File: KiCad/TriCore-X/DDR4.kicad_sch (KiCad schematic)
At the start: 2 parts, among them U1 RK3568B2, U8 IS43LQ32256AL-062BLI

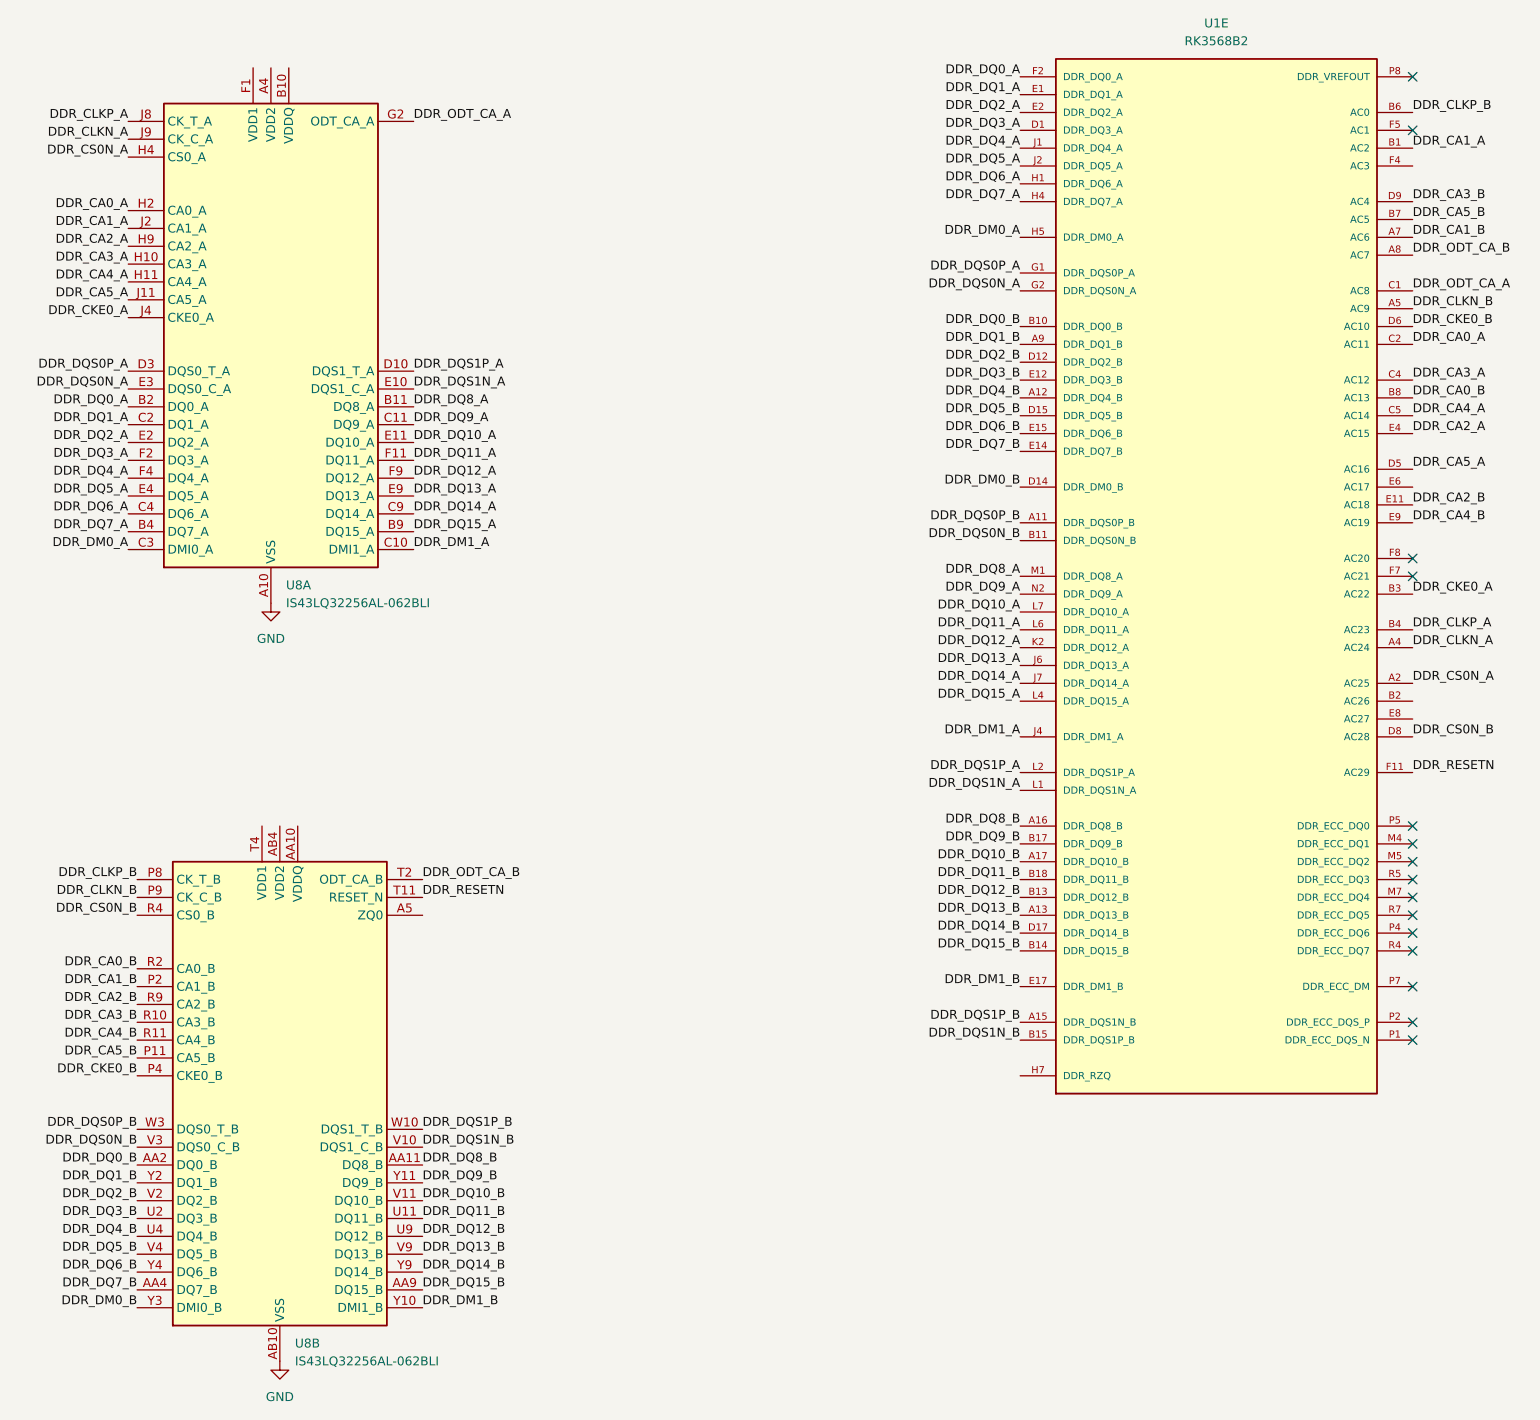
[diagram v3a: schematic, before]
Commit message: feat: complete schematic for RK809-5 PMIC peripheral circuits
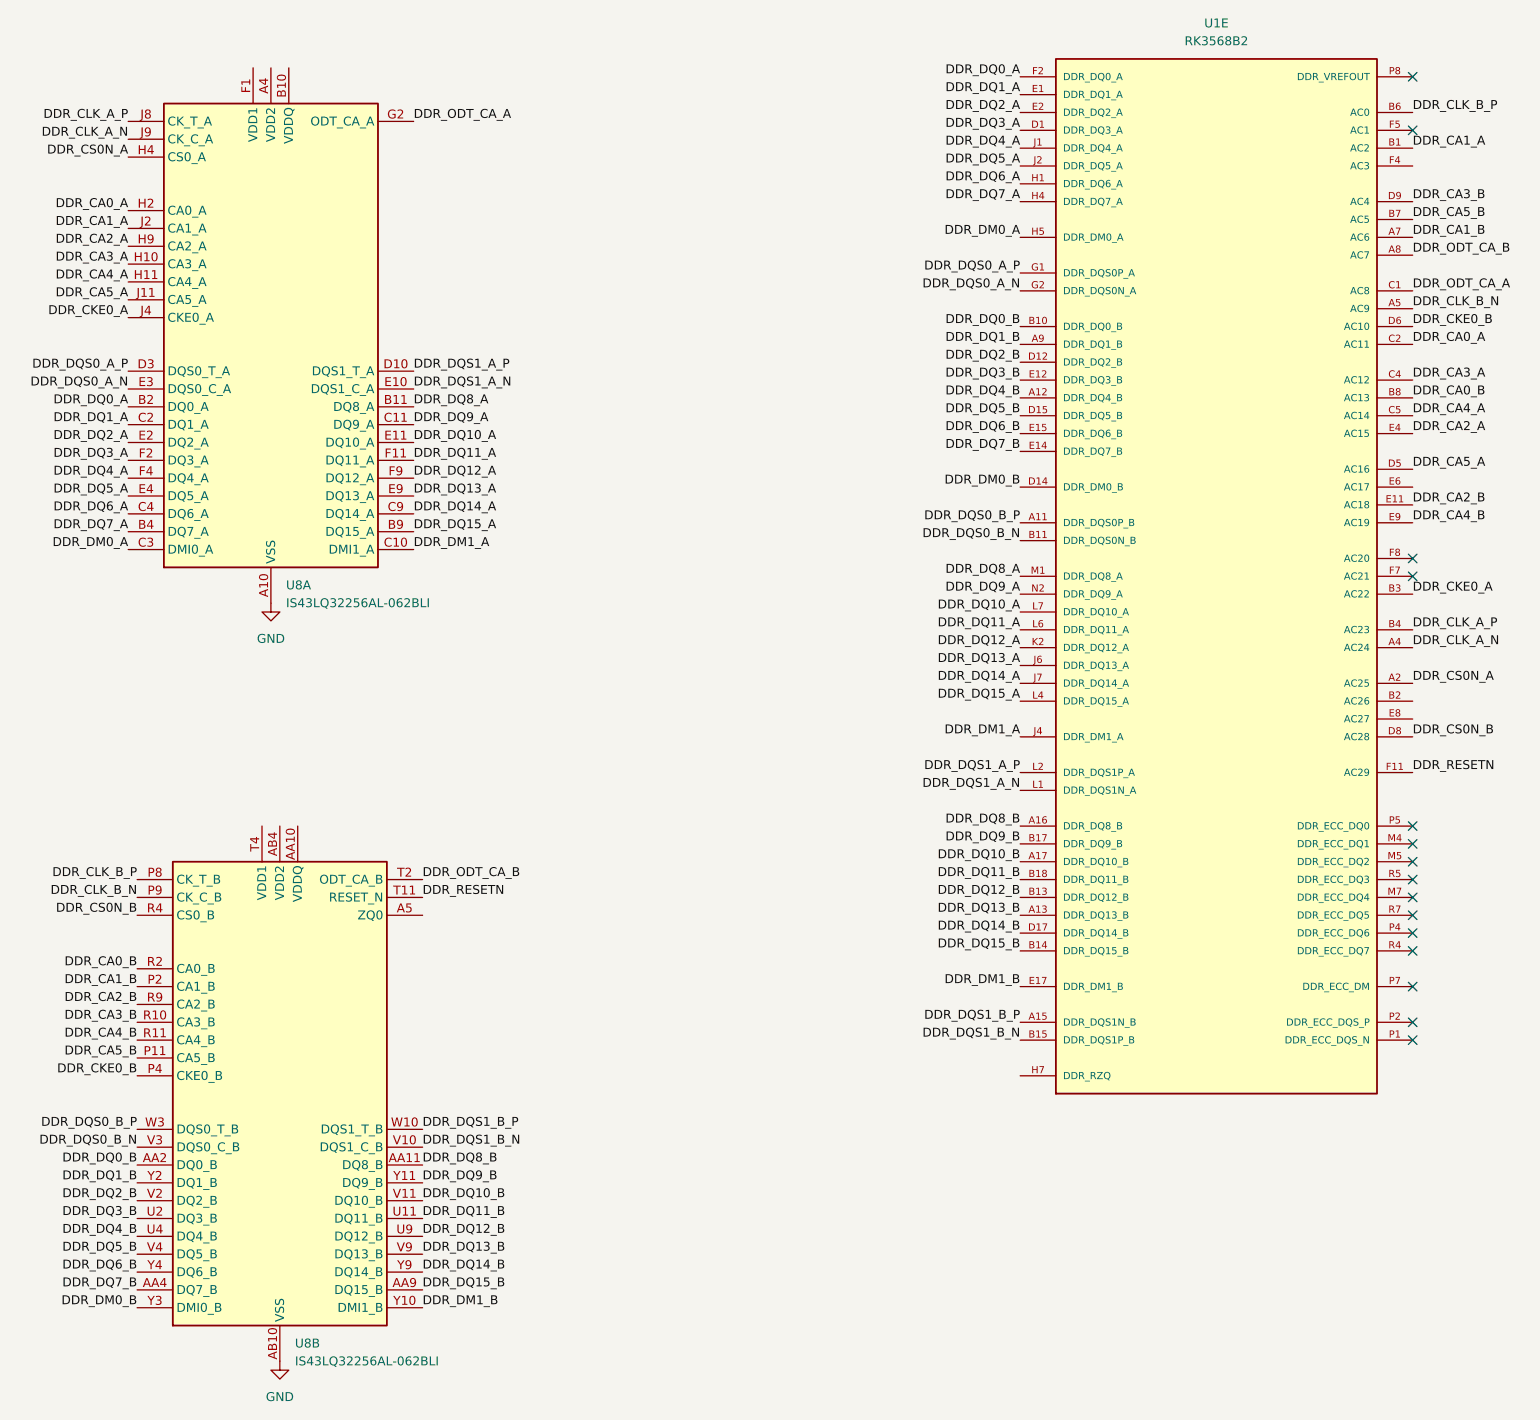
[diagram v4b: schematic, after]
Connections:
- net DDR_CLKN_A renamed DDR_CLK_A_N
- net DDR_CLKN_B renamed DDR_CLK_B_N
- net DDR_CLKP_A renamed DDR_CLK_A_P
- net DDR_CLKP_B renamed DDR_CLK_B_P
- net DDR_DQS0N_A renamed DDR_DQS0_A_N
- net DDR_DQS0N_B renamed DDR_DQS0_B_N
- net DDR_DQS0P_A renamed DDR_DQS0_A_P
- net DDR_DQS0P_B renamed DDR_DQS0_B_P
- net DDR_DQS1N_A renamed DDR_DQS1_A_N
- net DDR_DQS1N_B renamed DDR_DQS1_B_N
- net DDR_DQS1P_A renamed DDR_DQS1_A_P
- net DDR_DQS1P_B renamed DDR_DQS1_B_P
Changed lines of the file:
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@@
 		)
 	)
-	(label "DDR_DQS1N_B"
+	(label "DDR_DQS1_B_N"
 		(at 181.61 167.64 180)
 		(effects
@@
 		)
 	)
-	(label "DDR_CLKN_A"
+	(label "DDR_CLK_A_N"
 		(at 237.49 111.76 0)
 		(effects
@@
 		)
 	)
-	(label "DDR_DQS0P_B"
+	(label "DDR_DQS0_B_P"
 		(at 181.61 93.98 180)
 		(effects
@@
 		)
 	)
-	(label "DDR_DQS1N_B"
+	(label "DDR_DQS1_B_N"
 		(at 96.52 182.88 0)
 		(effects
@@
 		)
 	)
-	(label "DDR_DQS0N_A"
+	(label "DDR_DQS0_A_N"
 		(at 181.61 60.96 180)
 		(effects
@@
 		)
 	)
-	(label "DDR_DQS1P_A"
+	(label "DDR_DQS1_A_P"
 		(at 95.25 72.39 0)
 		(effects
@@
 		)
 	)
-	(label "DDR_DQS0N_B"
+	(label "DDR_DQS0_B_N"
 		(at 181.61 96.52 180)
 		(effects
@@
 		)
 	)
-	(label "DDR_DQS1N_A"
+	(label "DDR_DQS1_A_N"
 		(at 95.25 74.93 0)
 		(effects
@@
 		)
 	)
-	(label "DDR_CLKN_B"
+	(label "DDR_CLK_B_N"
 		(at 237.49 63.5 0)
 		(effects
@@
 		)
 	)
-	(label "DDR_CLKP_A"
+	(label "DDR_CLK_A_P"
 		(at 54.61 36.83 180)
 		(effects
@@
 		)
 	)
-	(label "DDR_DQS1P_B"
+	(label "DDR_DQS1_B_P"
 		(at 181.61 165.1 180)
 		(effects
@@
 		)
 	)
-	(label "DDR_DQS1P_B"
+	(label "DDR_DQS1_B_P"
 		(at 96.52 180.34 0)
 		(effects
@@
 		)
 	)
-	(label "DDR_DQS0P_A"
+	(label "DDR_DQS0_A_P"
 		(at 54.61 72.39 180)
 		(effects
@@
 		)
 	)
-	(label "DDR_CLKP_B"
+	(label "DDR_CLK_B_P"
 		(at 55.88 144.78 180)
 		(effects
@@
 		)
 	)
-	(label "DDR_DQS0P_A"
+	(label "DDR_DQS0_A_P"
 		(at 181.61 58.42 180)
 		(effects
@@
 		)
 	)
-	(label "DDR_CLKP_A"
+	(label "DDR_CLK_A_P"
 		(at 237.49 109.22 0)
 		(effects
@@
 		)
 	)
-	(label "DDR_DQS1P_A"
+	(label "DDR_DQS1_A_P"
 		(at 181.61 129.54 180)
 		(effects
@@
 		)
 	)
-	(label "DDR_DQS0N_A"
+	(label "DDR_DQS0_A_N"
 		(at 54.61 74.93 180)
 		(effects
@@
 		)
 	)
-	(label "DDR_DQS0N_B"
+	(label "DDR_DQS0_B_N"
 		(at 55.88 182.88 180)
 		(effects
@@
 		)
 	)
-	(label "DDR_CLKN_B"
+	(label "DDR_CLK_B_N"
 		(at 55.88 147.32 180)
 		(effects
@@
 		)
 	)
-	(label "DDR_CLKN_A"
+	(label "DDR_CLK_A_N"
 		(at 54.61 39.37 180)
 		(effects
@@
 		)
 	)
-	(label "DDR_DQS0P_B"
+	(label "DDR_DQS0_B_P"
 		(at 55.88 180.34 180)
 		(effects
@@
 		)
 	)
-	(label "DDR_CLKP_B"
+	(label "DDR_CLK_B_P"
 		(at 237.49 35.56 0)
 		(effects
@@
 		)
 	)
-	(label "DDR_DQS1N_A"
+	(label "DDR_DQS1_A_N"
 		(at 181.61 132.08 180)
 		(effects
